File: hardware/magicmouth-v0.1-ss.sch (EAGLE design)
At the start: 34 parts, among them IC1 LM386N, IC2 ATMEGA168-20P, Q1 16Mhz, U1 ARDUINOR3-NOIOREF-NOTEXT

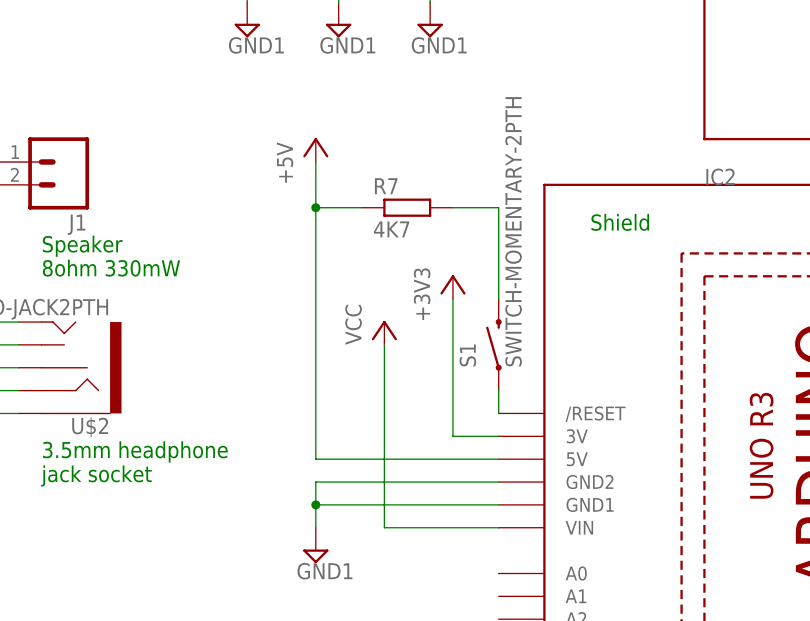
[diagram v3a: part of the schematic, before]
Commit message: connected reset button to GND not +5V
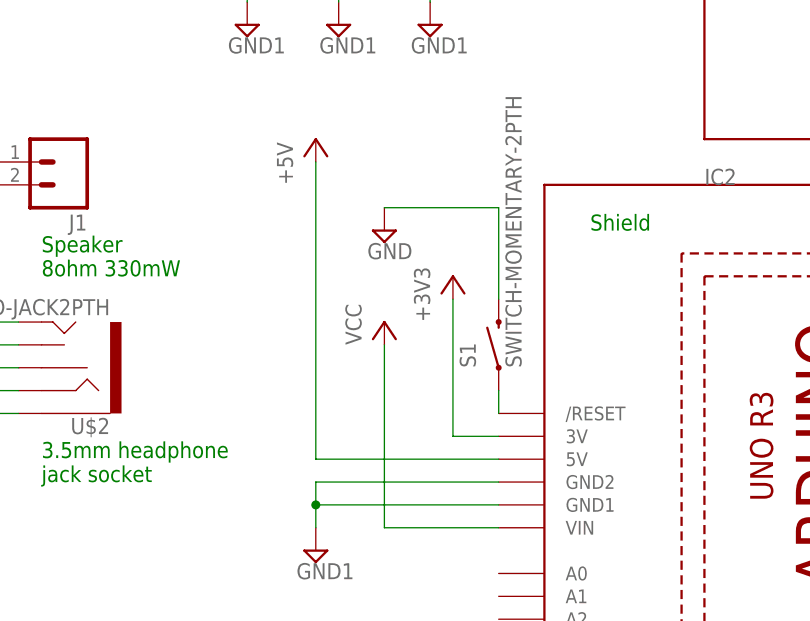
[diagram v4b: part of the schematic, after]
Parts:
- removed R7: 4K7, rcl:R-EU_0207/7
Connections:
- removed net N$34: R7.2, S1.2
- net +5V: no longer R7.1
- net GND: now also S1.2
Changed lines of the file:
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@@
 <part name="U$2" library="SparkFun-Connectors" deviceset="AUDIO-JACK2" device="PTH"/>
 <part name="S1" library="SparkFun-Electromechanical" deviceset="SWITCH-MOMENTARY-2" device="PTH"/>
-<part name="R7" library="rcl" deviceset="R-EU_" device="0207/7" value="4K7">
-<attribute name="RESISTANCE" value="4K7"/>
-</part>
 <part name="JP9" library="SparkFun-Connectors" deviceset="M01" device="SMDNS" value="M01SMDNS"/>
 <part name="R8" library="rcl" deviceset="R-EU_" device="0207/7" value="220K"/>
+<part name="GND7" library="supply2" deviceset="GND" device=""/>
 </parts>
 <sheets>
@@
 <instance part="U$2" gate="G$1" x="111.76" y="40.64" rot="R180"/>
 <instance part="S1" gate="G$1" x="160.02" y="43.18" rot="R90"/>
-<instance part="R7" gate="G$1" x="149.86" y="58.42"/>
 <instance part="JP9" gate="G$1" x="254" y="55.88" rot="R90"/>
 <instance part="R8" gate="G$1" x="40.64" y="83.82" rot="R270"/>
+<instance part="GND7" gate="GND" x="147.32" y="55.88"/>
 </instances>
 <busses>
@@
 <pinref part="R3" gate="G$1" pin="A"/>
 <wire x1="40.64" y1="58.293" x2="40.64" y2="43.18" width="0.1524" layer="91"/>
+</segment>
+<segment>
+<pinref part="S1" gate="G$1" pin="2"/>
+<wire x1="160.02" y1="58.42" x2="160.02" y2="48.26" width="0.1524" layer="91"/>
+<pinref part="GND7" gate="GND" pin="GND"/>
+<wire x1="147.32" y1="58.42" x2="160.02" y2="58.42" width="0.1524" layer="91"/>
 </segment>
 </net>
@@
 <wire x1="160.02" y1="30.48" x2="139.7" y2="30.48" width="0.1524" layer="91"/>
 <pinref part="P+5" gate="1" pin="+5V"/>
-<wire x1="139.7" y1="63.5" x2="139.7" y2="58.42" width="0.1524" layer="91"/>
-<pinref part="R7" gate="G$1" pin="1"/>
-<wire x1="139.7" y1="58.42" x2="139.7" y2="30.48" width="0.1524" layer="91"/>
-<wire x1="144.78" y1="58.42" x2="139.7" y2="58.42" width="0.1524" layer="91"/>
-<junction x="139.7" y="58.42"/>
+<wire x1="139.7" y1="63.5" x2="139.7" y2="30.48" width="0.1524" layer="91"/>
 </segment>
 <segment>
@@
 </segment>
 </net>
-<net name="N$34" class="0">
-<segment>
-<pinref part="R7" gate="G$1" pin="2"/>
-<pinref part="S1" gate="G$1" pin="2"/>
-<wire x1="154.94" y1="58.42" x2="160.02" y2="58.42" width="0.1524" layer="91"/>
-<wire x1="160.02" y1="58.42" x2="160.02" y2="48.26" width="0.1524" layer="91"/>
-</segment>
-</net>

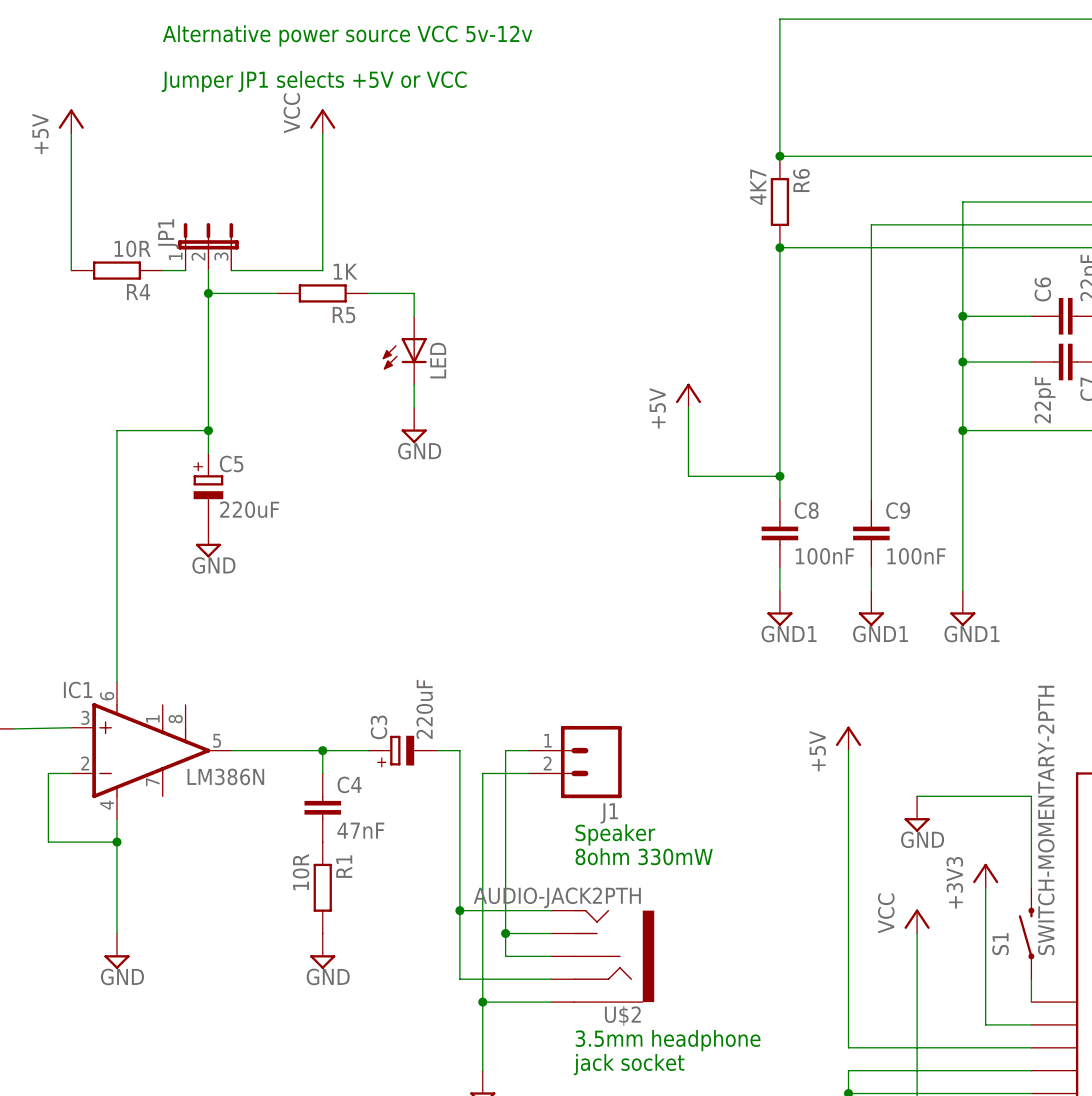
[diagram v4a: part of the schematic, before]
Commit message: adjusted placement to avoid through holes directly above Arduino USB port
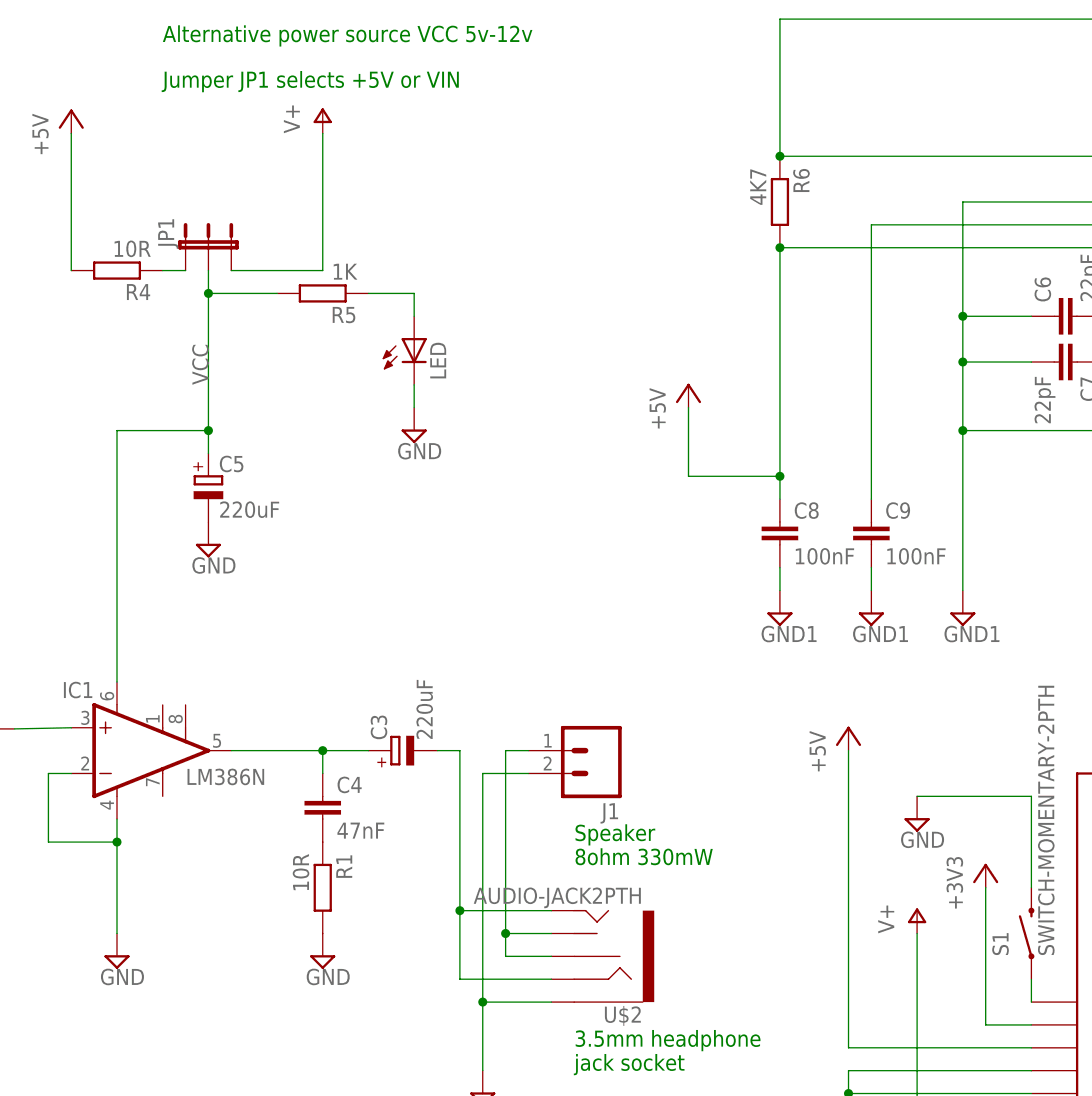
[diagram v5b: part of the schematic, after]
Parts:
- JP1: value (none) -> JUMPER-3PTH; device jumper:JP2E -> SparkFun-Passives:JUMPER-3PTH
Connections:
- removed net VS: C5.+, IC1.VS, JP1.2, R5.2
- new net VIN: JP1.3, U1.VIN
- net VCC: now also C5.+, IC1.VS, JP1.2, R5.2; no longer JP1.3, U1.VIN
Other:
- note added: "Jumper JP1 selects +5V or VIN"
- note removed: "Jumper JP1 selects +5V or VCC"
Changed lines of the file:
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@@
 <part name="C5" library="rcl" deviceset="CPOL-EU" device="TT5D7L" value="220uF"/>
 <part name="GND3" library="supply2" deviceset="GND" device=""/>
-<part name="JP1" library="jumper" deviceset="JP2E" device=""/>
 <part name="R5" library="rcl" deviceset="R-EU_" device="0207/7" value="1K"/>
 <part name="LED" library="led" deviceset="LED" device="3MM"/>
@@
 <part name="GND13" library="supply2" deviceset="GND1" device=""/>
 <part name="JP2" library="adafruit" deviceset="PINHD-1X8" device="CLEANBIG"/>
-<part name="P+1" library="supply1" deviceset="VCC" device=""/>
-<part name="P+2" library="supply1" deviceset="VCC" device=""/>
+<part name="P+1" library="supply1" deviceset="V+" device=""/>
+<part name="P+2" library="supply1" deviceset="V+" device=""/>
 <part name="GND14" library="supply2" deviceset="GND" device=""/>
 <part name="JP4" library="adafruit" deviceset="PINHD-1X6" device="CB"/>
@@
 <part name="R8" library="rcl" deviceset="R-EU_" device="0207/7" value="220K"/>
 <part name="GND7" library="supply2" deviceset="GND" device=""/>
+<part name="JP1" library="SparkFun-Passives" deviceset="JUMPER-3" device="PTH"/>
 </parts>
 <sheets>
@@
 <text x="109.22" y="50.8" size="1.778" layer="91">Speaker
 8ohm 330mW</text>
-<text x="63.5" y="137.16" size="1.778" layer="91">Jumper JP1 selects +5V or VCC</text>
+<text x="63.5" y="137.16" size="1.778" layer="91">Jumper JP1 selects +5V or VIN</text>
 <text x="63.5" y="142.24" size="1.778" layer="91">Alternative power source VCC 5v-12v</text>
 <text x="170.18" y="55.88" size="1.778" layer="91">Shield</text>
@@
 <instance part="C5" gate="G$1" x="68.58" y="93.98"/>
 <instance part="GND3" gate="GND" x="68.58" y="86.36"/>
-<instance part="JP1" gate="1" x="68.58" y="119.38"/>
 <instance part="R5" gate="G$1" x="81.28" y="114.3" rot="R180"/>
 <instance part="LED" gate="G$1" x="91.44" y="109.22"/>
@@
 <instance part="GND13" gate="G$1" x="139.7" y="20.32"/>
 <instance part="JP2" gate="G$1" x="269.24" y="96.52"/>
-<instance part="P+1" gate="VCC" x="147.32" y="45.72"/>
-<instance part="P+2" gate="VCC" x="81.28" y="134.62"/>
+<instance part="P+1" gate="1" x="147.32" y="45.72"/>
+<instance part="P+2" gate="1" x="81.28" y="134.62"/>
 <instance part="GND14" gate="GND" x="236.22" y="20.32"/>
 <instance part="JP4" gate="A" x="269.24" y="121.92"/>
@@
 <instance part="R8" gate="G$1" x="40.64" y="83.82" rot="R270"/>
 <instance part="GND7" gate="GND" x="147.32" y="55.88"/>
+<instance part="JP1" gate="G$1" x="66.04" y="119.38" smashed="yes">
+<attribute name="NAME" x="64.77" y="119.38" size="1.778" layer="95" rot="R90"/>
+</instance>
 </instances>
 <busses>
@@
 </segment>
 </net>
-<net name="VS" class="0">
+<net name="VCC" class="0">
 <segment>
 <wire x1="58.42" y1="71.12" x2="58.42" y2="99.06" width="0.1524" layer="91"/>
@@
 <pinref part="IC1" gate="G$1" pin="VS"/>
 <pinref part="C5" gate="G$1" pin="+"/>
-<pinref part="JP1" gate="1" pin="2"/>
 <pinref part="R5" gate="G$1" pin="2"/>
 <wire x1="68.58" y1="114.3" x2="68.58" y2="116.84" width="0.1524" layer="91"/>
 <wire x1="76.2" y1="114.3" x2="68.58" y2="114.3" width="0.1524" layer="91"/>
 <junction x="68.58" y="114.3"/>
+<pinref part="JP1" gate="G$1" pin="2"/>
+<label x="68.58" y="104.14" size="1.778" layer="95" rot="R90"/>
 </segment>
 </net>
@@
 <wire x1="66.04" y1="116.84" x2="63.5" y2="116.84" width="0.1524" layer="91"/>
 <pinref part="R4" gate="G$1" pin="1"/>
-<pinref part="JP1" gate="1" pin="1"/>
+<pinref part="JP1" gate="G$1" pin="1"/>
 </segment>
 </net>
@@
 </segment>
 </net>
-<net name="VCC" class="0">
+<net name="VIN" class="0">
 <segment>
 <pinref part="U1" gate="G$1" pin="VIN"/>
-<pinref part="P+1" gate="VCC" pin="VCC"/>
+<pinref part="P+1" gate="1" pin="V+"/>
 <wire x1="160.02" y1="22.86" x2="147.32" y2="22.86" width="0.1524" layer="91"/>
 <wire x1="147.32" y1="22.86" x2="147.32" y2="43.18" width="0.1524" layer="91"/>
@@
 <segment>
 <wire x1="71.12" y1="116.84" x2="81.28" y2="116.84" width="0.1524" layer="91"/>
-<pinref part="JP1" gate="1" pin="3"/>
-<pinref part="P+2" gate="VCC" pin="VCC"/>
+<pinref part="P+2" gate="1" pin="V+"/>
 <wire x1="81.28" y1="116.84" x2="81.28" y2="132.08" width="0.1524" layer="91"/>
-</segment>
-</net>
+<pinref part="JP1" gate="G$1" pin="3"/>
+</segment>
+</net>

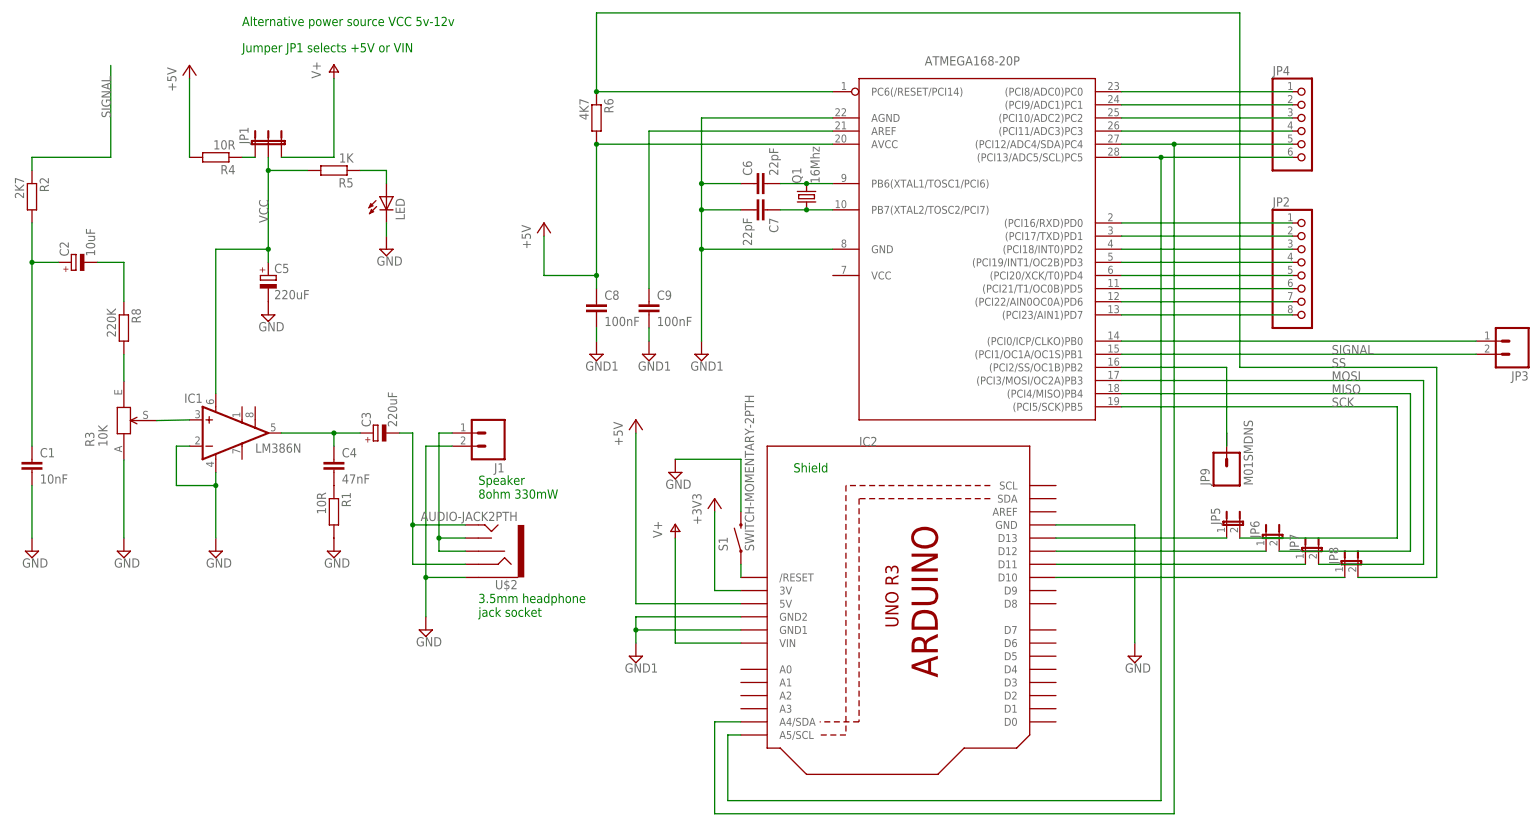
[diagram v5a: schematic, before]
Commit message: adjusted placement to avoid through holes directly above Arduino USB port
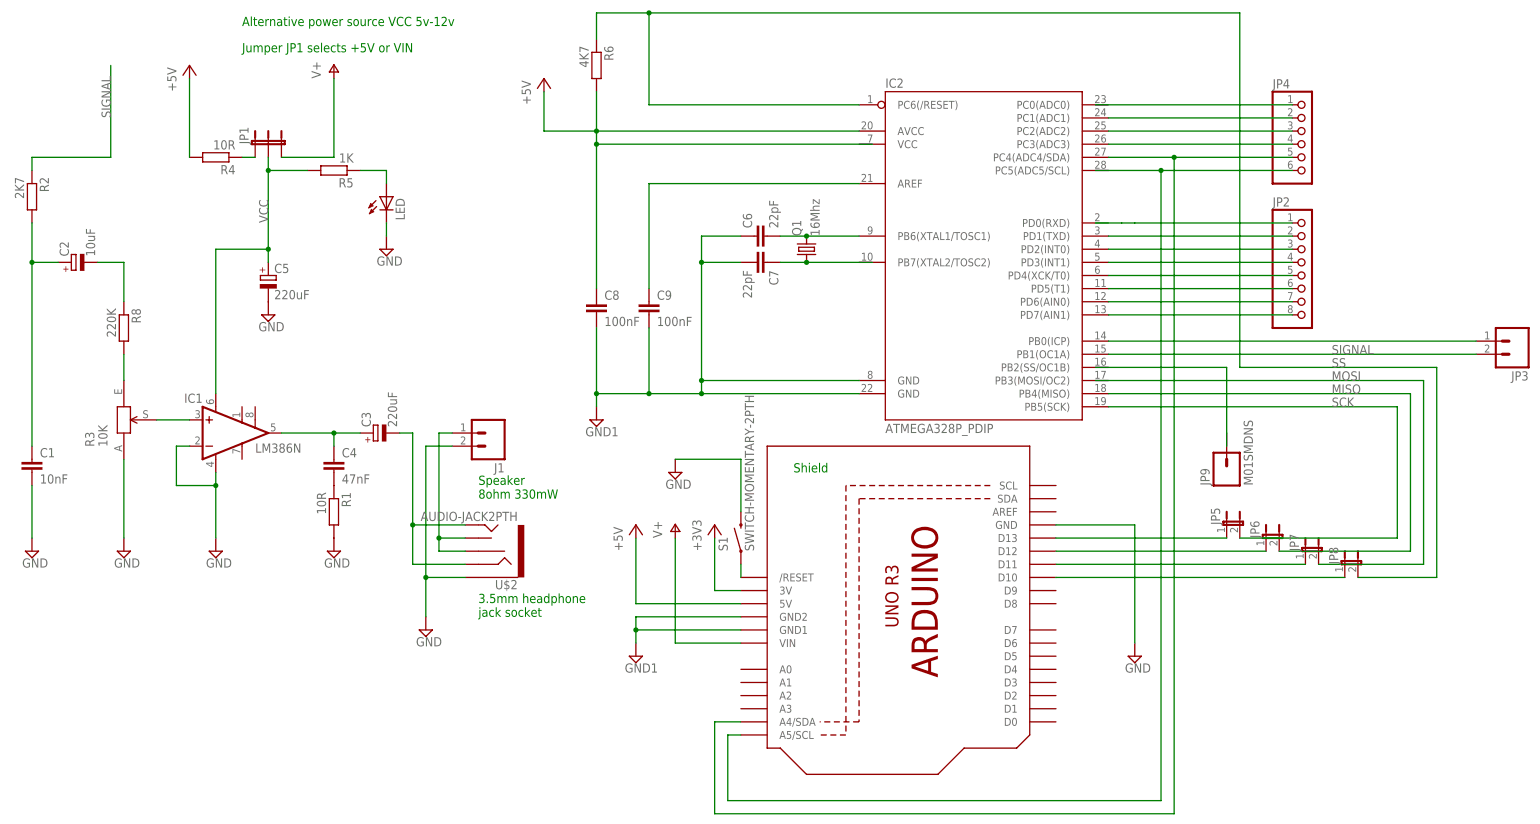
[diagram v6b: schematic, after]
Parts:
- IC2: value ATMEGA168-20P -> ATMEGA328P_PDIP; device adafruit:ATMEGA168-20P -> SparkFun-DigitalIC:ATMEGA328P_PDIP
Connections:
- net GND1: now also IC2.GND@1, IC2.GND@2; no longer IC2.AGND, IC2.GND
- net MISO: now also IC2.PB4(MISO); no longer IC2.(PCI4/MISO)PB4
- net MOSI: no longer IC2.(PCI3/MOSI/OC2A)PB3
- net N$11: no longer IC2.PB7(XTAL2/TOSC2/PCI7)
- net N$12: no longer IC2.(PCI2/SS/OC1B)PB2
- net N$13: no longer IC2.(PCI8/ADC0)PC0
- net N$15: now also IC2.PC1(ADC1); no longer IC2.(PCI9/ADC1)PC1
- net N$16: no longer IC2.(PCI16/RXD)PD0
- net N$17: now also IC2.PD1(TXD); no longer IC2.(PCI17/TXD)PD1
- net N$18: now also IC2.PD2(INT0); no longer IC2.(PCI18/INT0)PD2
- net N$19: now also IC2.PD3(INT1); no longer IC2.(PCI19/INT1/OC2B)PD3
- net N$20: now also IC2.PD4(XCK/T0); no longer IC2.(PCI20/XCK/T0)PD4
- net N$21: now also IC2.PD5(T1); no longer IC2.(PCI21/T1/OC0B)PD5
- net N$22: now also IC2.PD6(AIN0); no longer IC2.(PCI22/AIN0OC0A)PD6
- net N$23: now also IC2.PD7(AIN1); no longer IC2.(PCI23/AIN1)PD7
- net N$24: now also IC2.PB0(ICP); no longer IC2.(PCI0/ICP/CLKO)PB0
- net N$30: now also IC2.PC4(ADC4/SDA); no longer IC2.(PCI12/ADC4/SDA)PC4
- net N$31: no longer IC2.(PCI13/ADC5/SCL)PC5
- net N$32: now also IC2.PC2(ADC2); no longer IC2.(PCI10/ADC2)PC2
- net N$33: now also IC2.PC3(ADC3); no longer IC2.(PCI11/ADC3)PC3
- net N$6: now also IC2.PB6(XTAL1/TOSC1); no longer IC2.PB6(XTAL1/TOSC1/PCI6)
- net SCK: now also IC2.PB5(SCK); no longer IC2.(PCI5/SCK)PB5
- net SIGNAL: now also IC2.PB1(OC1A); no longer IC2.(PCI1/OC1A/OC1S)PB1
- net SS: now also IC2.PC6(/RESET); no longer IC2.PC6(/RESET/PCI14)
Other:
- moved on the sheet: C6, C7, IC2, JP4, Q1, R6
